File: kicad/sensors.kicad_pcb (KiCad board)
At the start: 2 copper layers, 84.1 x 61.7 mm, 58 parts, among them J1 Bus_PCI_Express_x1, J4 Conn_01x02, J6 USB_C_Receptacle_USB2.0_16P, U2 RP2040, U4 W25Q128JVP, U5 BMP388, U8 BNO055, U9 MCP25625T-E/ML, X1 ABM8-272-T3, Y1 ABS07-32.768KHZ-T, Y2 X322516MLB4SI

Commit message: update PCB editor
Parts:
- R1, R2: value 150 -> 1.5k
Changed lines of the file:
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@@
 		)
 		(property ki_fp_filters "WSON*1EP*6x5mm*P1.27mm*EP3.4x4.3mm*")
-		(sheetname "Root")
+		(sheetname "/")
 		(sheetfile "sensors.kicad_sch")
 		(attr smd)
@@
 		)
 		(property ki_fp_filters "C_*")
-		(sheetname "Root")
+		(sheetname "/")
 		(sheetfile "sensors.kicad_sch")
 		(attr smd)
@@
 		)
 		(property ki_fp_filters "R_*")
-		(sheetname "Root")
+		(sheetname "/")
 		(sheetfile "sensors.kicad_sch")
 		(attr smd)
@@
 			)
 		)
-		(sheetname "Root")
+		(sheetname "/")
 		(sheetfile "sensors.kicad_sch")
 		(attr smd)
@@
 		)
 		(property ki_fp_filters "R_*")
-		(sheetname "Root")
+		(sheetname "/")
 		(sheetfile "sensors.kicad_sch")
 		(attr smd)
@@
 		)
 		(property ki_fp_filters "C_*")
-		(sheetname "Root")
+		(sheetname "/")
 		(sheetfile "sensors.kicad_sch")
 		(attr smd)
@@
 		)
 		(property ki_fp_filters "C_*")
-		(sheetname "Root")
+		(sheetname "/")
 		(sheetfile "sensors.kicad_sch")
 		(attr smd)
@@
 		)
 		(property ki_fp_filters "C_*")
-		(sheetname "Root")
+		(sheetname "/")
 		(sheetfile "sensors.kicad_sch")
 		(attr smd)
@@
 			)
 		)
-		(sheetname "Root")
+		(sheetname "/")
 		(sheetfile "sensors.kicad_sch")
 		(attr smd)
@@
 			)
 		)
-		(sheetname "Root")
+		(sheetname "/")
 		(sheetfile "sensors.kicad_sch")
 		(attr smd)
@@
 			)
 		)
-		(property "Value" "150"
+		(property "Value" "1.5k"
 			(at 0 1.43 90)
 			(layer "F.Fab")
@@
 		)
 		(property ki_fp_filters "R_*")
-		(sheetname "Root")
+		(sheetname "/")
 		(sheetfile "sensors.kicad_sch")
 		(attr smd)
@@
 		)
 		(property ki_fp_filters "R_*")
-		(sheetname "Root")
+		(sheetname "/")
 		(sheetfile "sensors.kicad_sch")
 		(attr smd)
@@
 		)
 		(property ki_fp_filters "LED* LED_SMD:* LED_THT:*")
-		(sheetname "Root")
+		(sheetname "/")
 		(sheetfile "sensors.kicad_sch")
 		(attr smd)
@@
 		)
 		(property ki_fp_filters "C_*")
-		(sheetname "Root")
+		(sheetname "/")
 		(sheetfile "sensors.kicad_sch")
 		(attr smd)
@@
 		)
 		(property ki_fp_filters "QFN28_6X6MC_MCH QFN28_6X6MC_MCH-M QFN28_6X6MC_MCH-L")
-		(sheetname "Root")
+		(sheetname "/")
 		(sheetfile "sensors.kicad_sch")
 		(attr smd)
@@
 		)
 		(property ki_fp_filters "R_*")
-		(sheetname "Root")
+		(sheetname "/")
 		(sheetfile "sensors.kicad_sch")
 		(attr smd)
@@
 		)
 		(property ki_fp_filters "C_*")
-		(sheetname "Root")
+		(sheetname "/")
 		(sheetfile "sensors.kicad_sch")
 		(attr smd)
@@
 		)
 		(property ki_fp_filters "C_*")
-		(sheetname "Root")
+		(sheetname "/")
 		(sheetfile "sensors.kicad_sch")
 		(attr smd)
@@
 		)
 		(property ki_fp_filters "C_*")
-		(sheetname "Root")
+		(sheetname "/")
 		(sheetfile "sensors.kicad_sch")
 		(attr smd)
@@
 		)
 		(property ki_fp_filters "LED* LED_SMD:* LED_THT:*")
-		(sheetname "Root")
+		(sheetname "/")
 		(sheetfile "sensors.kicad_sch")
 		(attr smd)
@@
 			)
 		)
-		(property "Value" "150"
+		(property "Value" "1.5k"
 			(at 0 1.43 90)
 			(layer "F.Fab")
@@
 		)
 		(property ki_fp_filters "R_*")
-		(sheetname "Root")
+		(sheetname "/")
 		(sheetfile "sensors.kicad_sch")
 		(attr smd)
@@
 		)
 		(property ki_fp_filters "C_*")
-		(sheetname "Root")
+		(sheetname "/")
 		(sheetfile "sensors.kicad_sch")
 		(attr smd)
@@
 		)
 		(property ki_fp_filters "LED* LED_SMD:* LED_THT:*")
-		(sheetname "Root")
+		(sheetname "/")
 		(sheetfile "sensors.kicad_sch")
 		(attr smd)
@@
 		)
 		(property ki_fp_filters "C_*")
-		(sheetname "Root")
+		(sheetname "/")
 		(sheetfile "sensors.kicad_sch")
 		(attr smd)
@@
 		)
 		(property ki_fp_filters "R_*")
-		(sheetname "Root")
+		(sheetname "/")
 		(sheetfile "sensors.kicad_sch")
 		(attr smd)
@@
 		)
 		(property ki_fp_filters "C_*")
-		(sheetname "Root")
+		(sheetname "/")
 		(sheetfile "sensors.kicad_sch")
 		(attr smd)
@@
 		)
 		(property ki_fp_filters "USB*C*Receptacle*")
-		(sheetname "Root")
+		(sheetname "/")
 		(sheetfile "sensors.kicad_sch")
 		(attr smd)
@@
 		)
 		(property ki_fp_filters "ABM8-272-T3_ABR")
-		(sheetname "Root")
+		(sheetname "/")
 		(sheetfile "sensors.kicad_sch")
 		(attr smd)
@@
 		)
 		(property ki_fp_filters "C_*")
-		(sheetname "Root")
+		(sheetname "/")
 		(sheetfile "sensors.kicad_sch")
 		(attr smd)
@@
 		)
 		(property ki_fp_filters "C_*")
-		(sheetname "Root")
+		(sheetname "/")
 		(sheetfile "sensors.kicad_sch")
 		(attr smd)
@@
 		)
 		(property ki_fp_filters "C_*")
-		(sheetname "Root")
+		(sheetname "/")
 		(sheetfile "sensors.kicad_sch")
 		(attr smd)
@@
 		)
 		(property ki_fp_filters "R_*")
-		(sheetname "Root")
+		(sheetname "/")
 		(sheetfile "sensors.kicad_sch")
 		(attr smd)
@@
 		)
 		(property ki_fp_filters "C_*")
-		(sheetname "Root")
+		(sheetname "/")
 		(sheetfile "sensors.kicad_sch")
 		(attr smd)
@@
 		)
 		(property ki_fp_filters "C_*")
-		(sheetname "Root")
+		(sheetname "/")
 		(sheetfile "sensors.kicad_sch")
 		(attr smd)
@@
 		)
 		(property ki_fp_filters "C_*")
-		(sheetname "Root")
+		(sheetname "/")
 		(sheetfile "sensors.kicad_sch")
 		(attr smd)
@@
 		)
 		(property ki_fp_filters "LGA*5.2x3.8mm*P0.5mm*")
-		(sheetname "Root")
+		(sheetname "/")
 		(sheetfile "sensors.kicad_sch")
 		(attr smd)
@@
 		)
 		(property ki_fp_filters "R_*")
-		(sheetname "Root")
+		(sheetname "/")
 		(sheetfile "sensors.kicad_sch")
 		(attr smd)
@@
 			)
 		)
-		(sheetname "Root")
+		(sheetname "/")
 		(sheetfile "sensors.kicad_sch")
 		(attr smd)
@@
 		)
 		(property ki_fp_filters "C_*")
-		(sheetname "Root")
+		(sheetname "/")
 		(sheetfile "sensors.kicad_sch")
 		(attr smd)
@@
 		)
 		(property ki_fp_filters "R_*")
-		(sheetname "Root")
+		(sheetname "/")
 		(sheetfile "sensors.kicad_sch")
 		(attr smd)
@@
 		)
 		(property ki_fp_filters "R_*")
-		(sheetname "Root")
+		(sheetname "/")
 		(sheetfile "sensors.kicad_sch")
 		(attr smd)
@@
 		)
 		(property ki_fp_filters "QFN*1EP*7x7mm?P0.4mm*")
-		(sheetname "Root")
+		(sheetname "/")
 		(sheetfile "sensors.kicad_sch")
 		(attr smd)
@@
 		)
 		(property ki_fp_filters "C_*")
-		(sheetname "Root")
+		(sheetname "/")
 		(sheetfile "sensors.kicad_sch")
 		(attr smd)
@@
 		)
 		(property ki_fp_filters "R_*")
-		(sheetname "Root")
+		(sheetname "/")
 		(sheetfile "sensors.kicad_sch")
 		(attr smd)
@@
 		)
 		(property ki_fp_filters "R_*")
-		(sheetname "Root")
+		(sheetname "/")
 		(sheetfile "sensors.kicad_sch")
 		(attr smd)
@@
 		)
 		(property ki_fp_filters "C_*")
-		(sheetname "Root")
+		(sheetname "/")
 		(sheetfile "sensors.kicad_sch")
 		(attr smd)
@@
 		)
 		(property ki_fp_filters "Connector*:*_1x??_*")
-		(sheetname "Root")
+		(sheetname "/")
 		(sheetfile "sensors.kicad_sch")
 		(attr through_hole dnp)
@@
 		)
 		(property ki_fp_filters "R_*")
-		(sheetname "Root")
+		(sheetname "/")
 		(sheetfile "sensors.kicad_sch")
 		(attr smd)
@@
 		)
 		(property ki_fp_filters "C_*")
-		(sheetname "Root")
+		(sheetname "/")
 		(sheetfile "sensors.kicad_sch")
 		(attr smd)
@@
 		)
 		(property ki_fp_filters "C_*")
-		(sheetname "Root")
+		(sheetname "/")
 		(sheetfile "sensors.kicad_sch")
 		(attr smd)
@@
 		)
 		(property ki_fp_filters "C_*")
-		(sheetname "Root")
+		(sheetname "/")
 		(sheetfile "sensors.kicad_sch")
 		(attr smd)
@@
 			)
 		)
-		(sheetname "Root")
+		(sheetname "/")
 		(sheetfile "sensors.kicad_sch")
 		(attr smd)
@@
 		)
 		(property ki_fp_filters "C_*")
-		(sheetname "Root")
+		(sheetname "/")
 		(sheetfile "sensors.kicad_sch")
 		(attr smd)
@@
 		)
 		(property ki_fp_filters "R_*")
-		(sheetname "Root")
+		(sheetname "/")
 		(sheetfile "sensors.kicad_sch")
 		(attr smd)
@@
 		)
 		(property ki_fp_filters "C_*")
-		(sheetname "Root")
+		(sheetname "/")
 		(sheetfile "sensors.kicad_sch")
 		(attr smd)
@@
 		)
 		(property ki_fp_filters "R_*")
-		(sheetname "Root")
+		(sheetname "/")
 		(sheetfile "sensors.kicad_sch")
 		(attr smd)
@@
 		)
 		(property ki_fp_filters "C_*")
-		(sheetname "Root")
+		(sheetname "/")
 		(sheetfile "sensors.kicad_sch")
 		(attr smd)
@@
 		)
 		(property ki_fp_filters "*PCIexpress*")
-		(sheetname "Root")
+		(sheetname "/")
 		(sheetfile "sensors.kicad_sch")
 		(attr exclude_from_pos_files dnp)

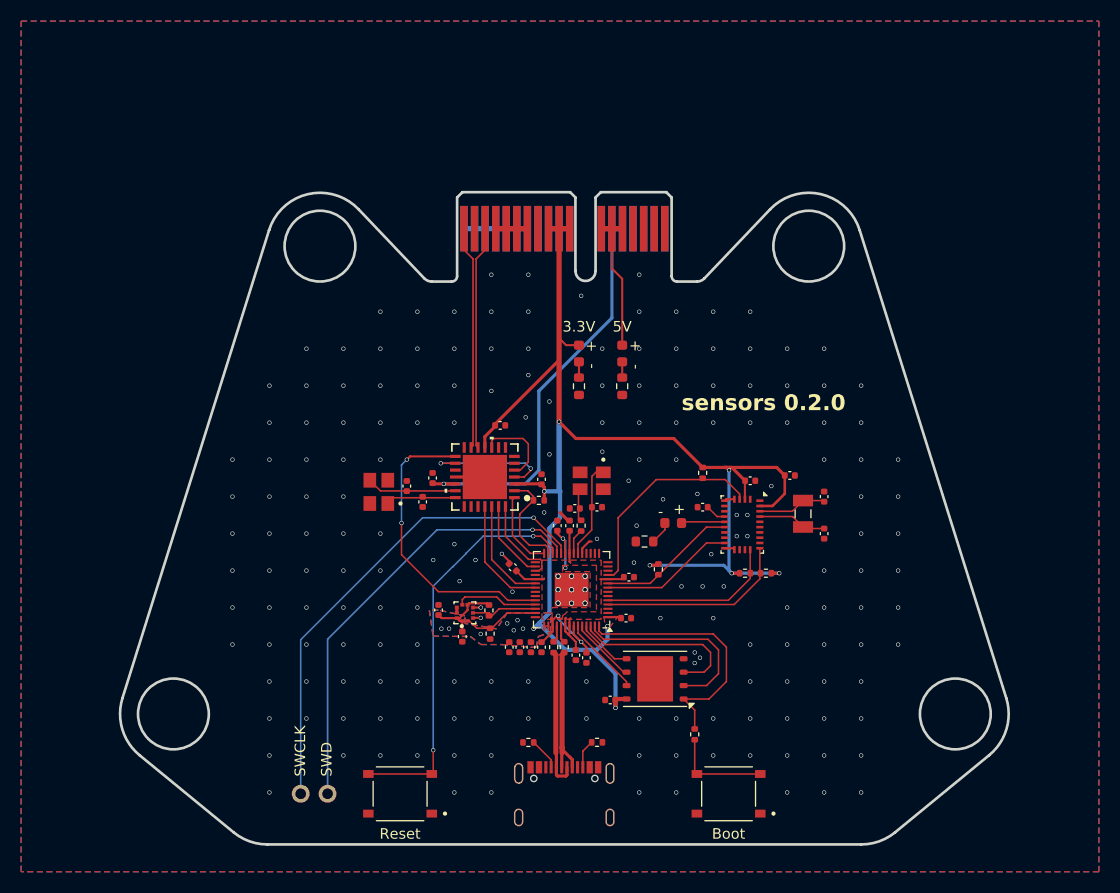
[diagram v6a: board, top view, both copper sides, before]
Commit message: move LEDs and text to bottom update to 0.2.1
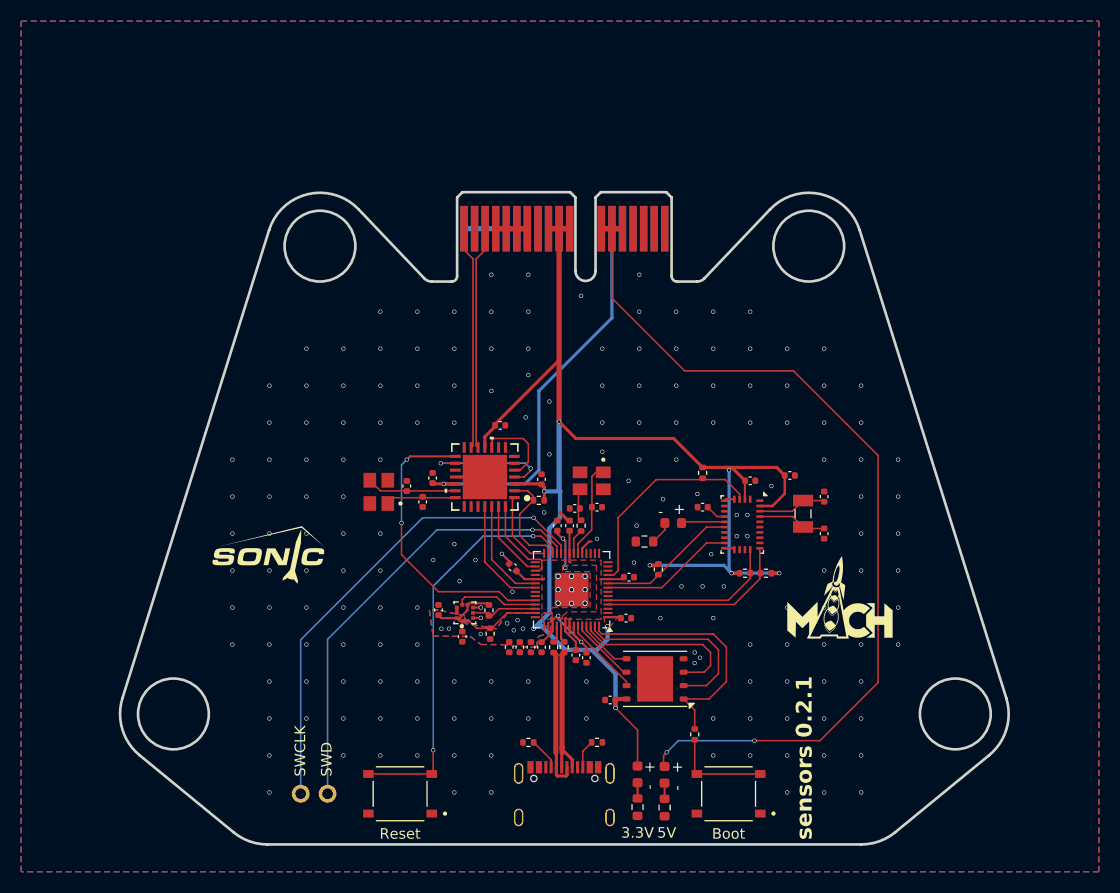
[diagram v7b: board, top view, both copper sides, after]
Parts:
- added G***: LOGO, LOGO, F.Cu at (172.5, 100.0)
- R89: value 150 -> 1.5k
- moved D1 40.2 mm to (153.3, 115.8)
- moved R1 40.2 mm to (153.3, 118.9)
- moved D2 40.1 mm to (155.9, 115.8)
- moved R2 40.1 mm to (155.9, 118.9)
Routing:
- net +5V: track 52.6 -> 124.8 mm, vias 1 -> 3
- net +3.3V: track 166.5 -> 170.7 mm
- net GND: vias 201 -> 195
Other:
- board text added: "sensors 0.2.1"
- board text removed: "sensors 0.2.0"
